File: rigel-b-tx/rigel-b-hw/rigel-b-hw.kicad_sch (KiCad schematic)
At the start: 57 parts, among them IC1 BALFHB-WL-02D3, J4 BCS-102-L-D-TE, J5 S2B-XH-A, U1 STM32WLE5C8Ux, U2 TPS629206DRLR, U3 CH340X, U4 TYPE-C_16PIN_2MD(073), U5 X1G004131004200, U6 KH-SMA-K513-G, U7 MSK12C02-HB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

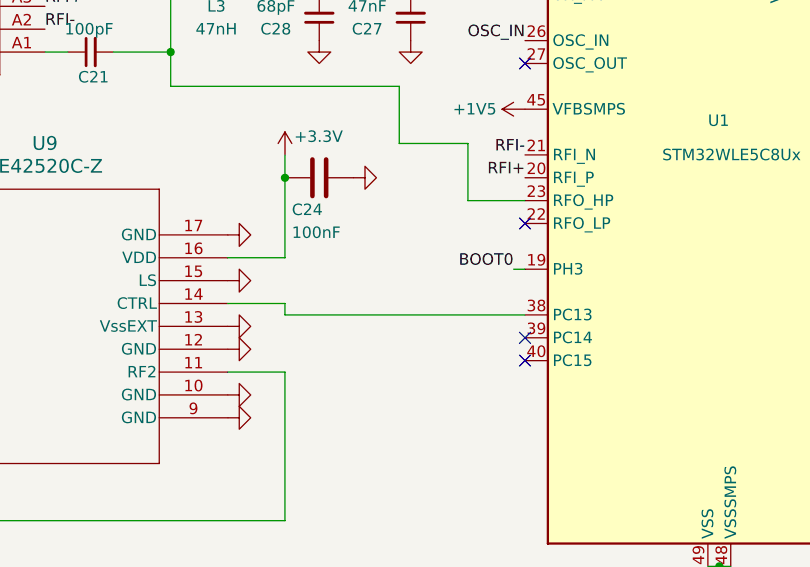
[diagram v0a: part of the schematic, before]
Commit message: Added a capacitor for the switch
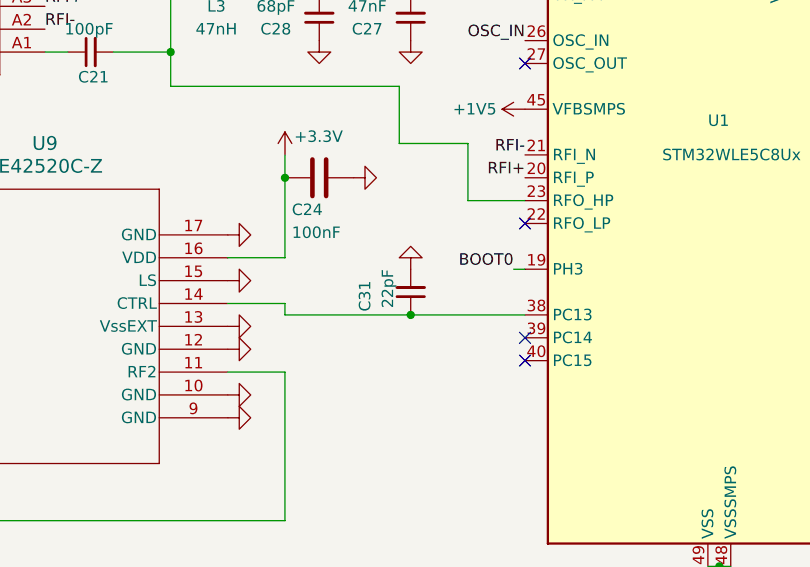
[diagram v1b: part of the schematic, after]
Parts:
- added C31: 22pF, Capacitor_SMD:C_0402_1005Metric, symbol Device:C_Small
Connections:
- net GND: now also C31.2
- net at U1.38 (PC13), U9.14 (CTRL): now also C31.1
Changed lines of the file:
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@@
 	)
 	(junction
+		(at 115.57 95.25)
+		(diameter 0)
+		(color 0 0 0 0)
+	)
+	(junction
 		(at 186.69 129.54)
 		(diameter 0)
@@
 	(wire
 		(pts
+			(xy 115.57 95.25) (xy 128.27 95.25)
+		)
+		(stroke
+			(width 0)
+			(type default)
+		)
+	)
+	(wire
+		(pts
 			(xy 147.32 27.94) (xy 148.59 27.94)
 		)
@@
 	(wire
 		(pts
-			(xy 101.6 95.25) (xy 128.27 95.25)
+			(xy 101.6 95.25) (xy 115.57 95.25)
 		)
 		(stroke
@@
 	)
 	(symbol
+		(lib_name "GND_7")
+		(lib_id "power:GND")
+		(at 115.57 90.17 180)
+		(unit 1)
+		(exclude_from_sim no)
+		(in_bom yes)
+		(on_board yes)
+		(dnp no)
+		(fields_autoplaced yes)
+		(property "Reference" "#PWR085"
+			(at 115.57 83.82 0)
+			(effects
+				(font
+					(size 1.27 1.27)
+				)
+				(hide yes)
+			)
+		)
+		(property "Value" "GND"
+			(at 115.57 85.09 0)
+			(effects
+				(font
+					(size 1.27 1.27)
+				)
+				(hide yes)
+			)
+		)
+		(property "Footprint" ""
+			(at 115.57 90.17 0)
+			(effects
+				(font
+					(size 1.27 1.27)
+				)
+				(hide yes)
+			)
+		)
+		(property "Datasheet" ""
+			(at 115.57 90.17 0)
+			(effects
+				(font
+					(size 1.27 1.27)
+				)
+				(hide yes)
+			)
+		)
+		(property "Description" "Power symbol creates a global label with name \"GND\" , ground"
+			(at 115.57 90.17 0)
+			(effects
+				(font
+					(size 1.27 1.27)
+				)
+				(hide yes)
+			)
+		)
+		(pin "1"
+		)
+		(instances
+			(project "rigel-b-hw"
+				(path "/5b772f1b-b884-4184-9180-5f1d0867ded9"
+					(reference "#PWR085")
+					(unit 1)
+				)
+			)
+		)
+	)
+	(symbol
 		(lib_id "power:GND")
 		(at 139.7 163.83 270)
@@
 					(unit 1)
 				)
+			)
+		)
+	)
+	(symbol
+		(lib_id "Device:C_Small")
+		(at 115.57 92.71 180)
+		(unit 1)
+		(exclude_from_sim no)
+		(in_bom yes)
+		(on_board yes)
+		(dnp no)
+		(property "Reference" "C31"
+			(at 110.49 91.44 90)
+			(effects
+				(font
+					(size 1.27 1.27)
+				)
+				(justify left)
+			)
+		)
+		(property "Value" "22pF"
+			(at 113.03 90.17 90)
+			(effects
+				(font
+					(size 1.27 1.27)
+				)
+				(justify left)
+			)
+		)
+		(property "Footprint" "Capacitor_SMD:C_0402_1005Metric"
+			(at 115.57 92.71 0)
+			(effects
+				(font
+					(size 1.27 1.27)
+				)
+				(hide yes)
+			)
+		)
+		(property "Datasheet" "~"
+			(at 115.57 92.71 0)
+			(effects
+				(font
+					(size 1.27 1.27)
+				)
+				(hide yes)
+			)
+		)
+		(property "Description" ""
+			(at 115.57 92.71 0)
+			(effects
+				(font
+					(size 1.27 1.27)
+				)
+				(hide yes)
+			)
+		)
+		(pin "1"
+		)
+		(pin "2"
+		)
+		(instances
+			(project "rigel-b-hw"
+				(path "/5b772f1b-b884-4184-9180-5f1d0867ded9"
+					(reference "C31")
+					(unit 1)
+				)

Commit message: New Switch
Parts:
- removed U9: PE42520C-Z, QFN_2520C-Z_PSM, symbol 2025-02-07_21-48-15:PE42520C-Z
- added U10: 4259-63, jlc:SC-70-6_PSM, symbol 2025-02-21_03-29-19:4259-63
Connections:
- net +3.3V: now also U10.6 (*CTRL/VDD)
- net GND: now also U10.2 (GND)
- net at C20.2, IC1.C3 (RFI_IN): now also U10.1 (RF1)
- net at C1.1: now also U10.5 (RFC)
- net at C31.1, U1.38 (PC13): now also U10.4 (CTRL)
- net at C22.1: now also U10.3 (RF2)
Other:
- moved on the sheet: C1, C24, C31, U6

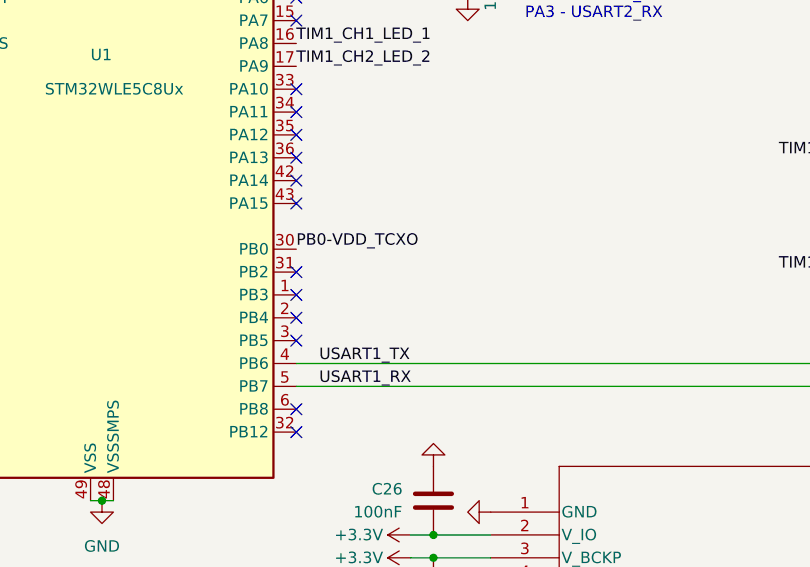
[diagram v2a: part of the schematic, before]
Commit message: connected PB2 and PB3 to Data 1 and Data 2 (for data transfer from Polaris)
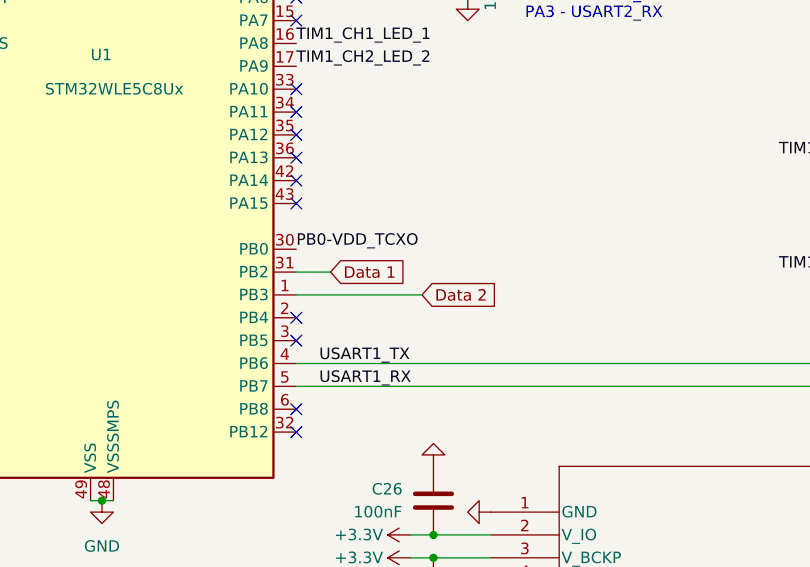
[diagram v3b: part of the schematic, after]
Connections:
- net Data 1: now also U1.31 (PB2)
- net Data 2: now also U1.1 (PB3)
- no-connect marks 35 -> 33
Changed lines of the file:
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@@
-	)
-	(no_connect
-		(at 171.45 97.79)
 	)
 	(no_connect
@@
 	)
 	(no_connect
-		(at 171.45 100.33)
-	)
-	(no_connect
 		(at 128.27 85.09)
 	)
@@
 	(wire
 		(pts
+			(xy 171.45 100.33) (xy 185.42 100.33)
+		)
+		(stroke
+			(width 0)
+			(type default)
+		)
+	)
+	(wire
+		(pts
 			(xy 147.32 181.61) (xy 135.89 181.61)
 		)
@@
 		(pts
 			(xy 190.5 59.69) (xy 193.04 59.69)
+		)
+		(stroke
+			(width 0)
+			(type default)
+		)
+	)
+	(wire
+		(pts
+			(xy 171.45 97.79) (xy 175.26 97.79)
 		)
 		(stroke
@@
 				(hide yes)
 			)
+		)
+	)
+	(global_label "Data 2"
+		(shape input)
+		(at 185.42 100.33 0)
+		(fields_autoplaced yes)
+		(effects
+			(font
+				(size 1.27 1.27)
+			)
+			(justify left)
+		)
+		(property "Intersheetrefs" "${INTERSHEET_REFS}"
+			(at 194.876 100.33 0)
+			(effects
+				(font
+					(size 1.27 1.27)
+				)
+				(justify left)
+				(hide yes)
+			)
+		)
+	)
+	(global_label "Data 1"
+		(shape input)
+		(at 175.26 97.79 0)
+		(fields_autoplaced yes)
+		(effects
+			(font
+				(size 1.27 1.27)
+			)
+			(justify left)
+		)
+		(property "Intersheetrefs" "${INTERSHEET_REFS}"
+			(at 184.716 97.79 0)
+			(effects
+				(font
+					(size 1.27 1.27)
+				)
+				(justify left)
+				(hide yes)
+			)
